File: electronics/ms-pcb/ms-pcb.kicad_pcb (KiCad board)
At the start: 2 copper layers, 110 x 110 mm, 25 parts, among them J1 Left motor, J2 Right motor, J3 XT60-M, U1 ESP32-S3-DEVKITC-1U-N8R2, U2 GY-521

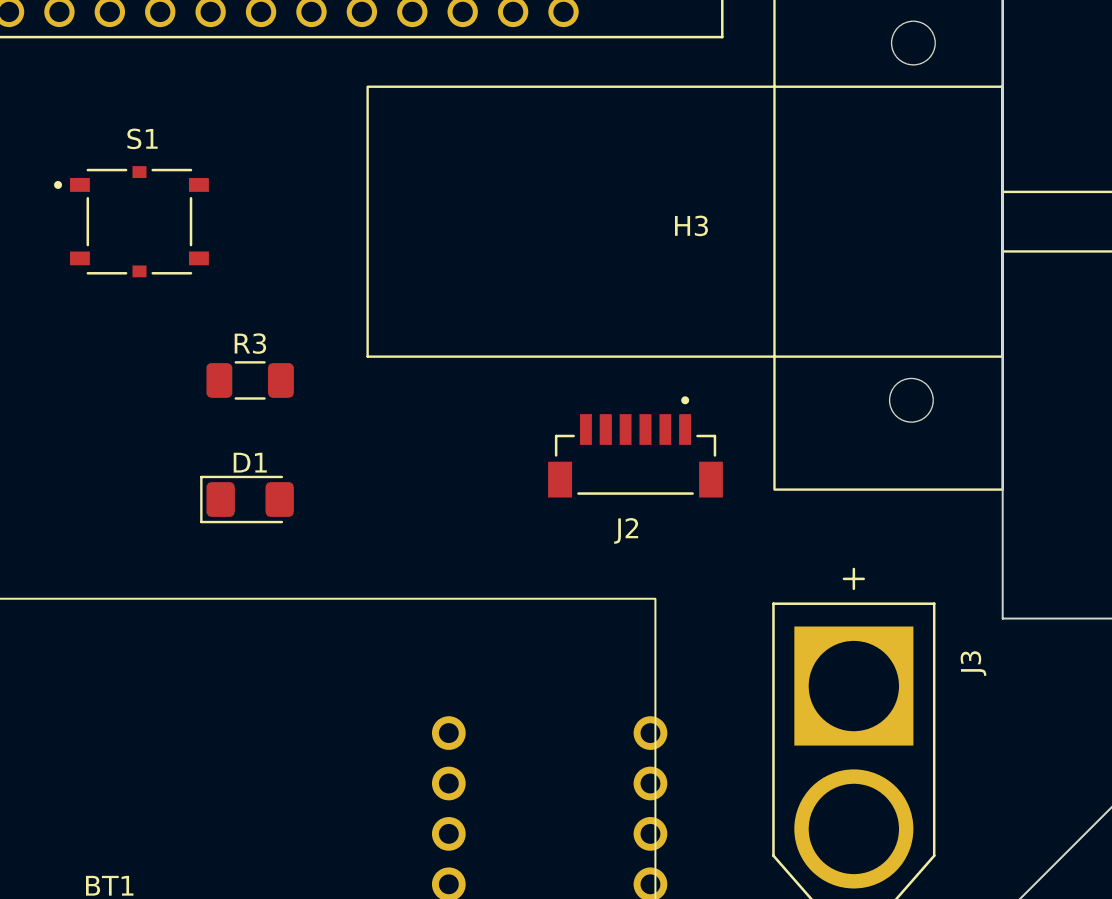
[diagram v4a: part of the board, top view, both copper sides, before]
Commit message: elec: enhance PCB v0.1 layout
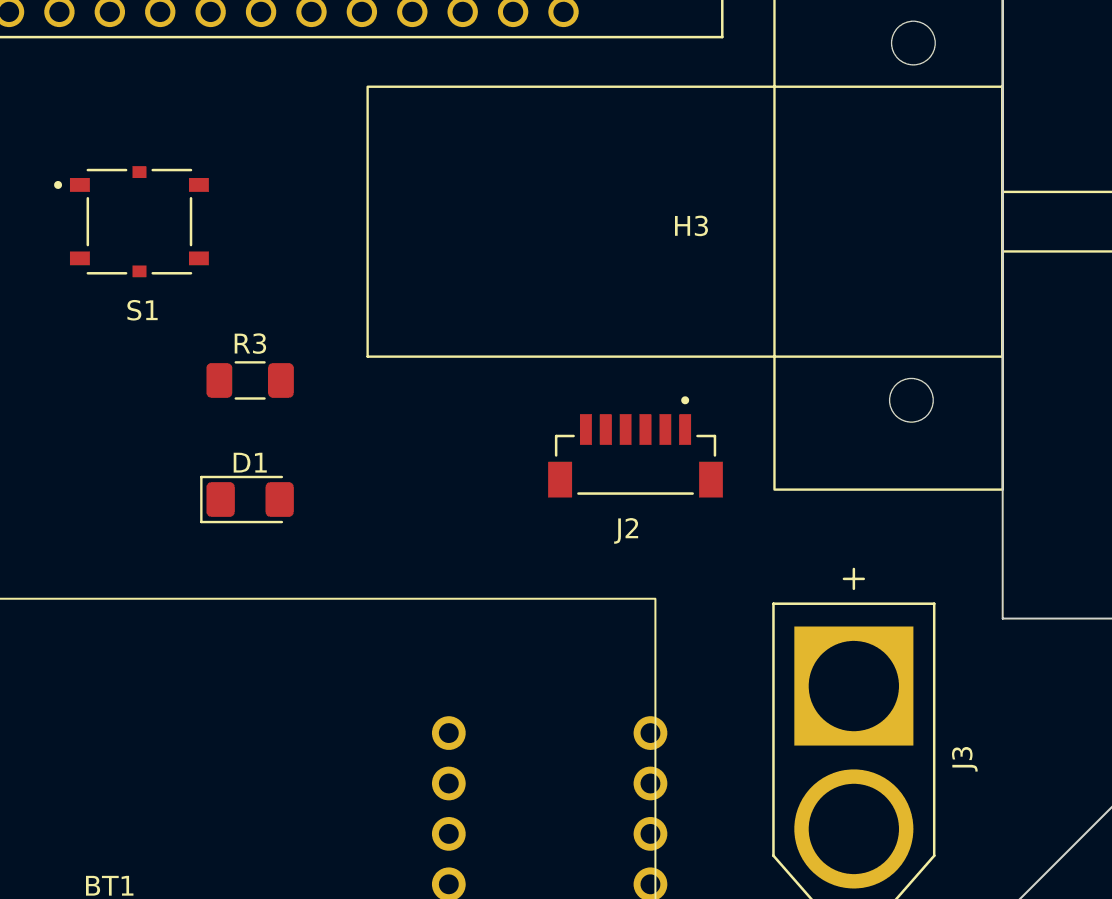
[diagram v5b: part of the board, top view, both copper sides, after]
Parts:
- H2, H4: footprint footprints:caster_wheel -> footprints:caster_wheel_custom
- renumbered DRV1 to DRV8833, LS1 to PKLCS1212E20A0-R1
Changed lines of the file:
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@@
 			)
 		)
-		(property "Description" ""
+		(property "Description" "\nConnector Header Surface Mount 6 position 0.039 (1.00mm)\n"
 			(at 98.500006 108.000013 0)
 			(layer "F.Fab")
@@
 			)
 		)
-		(property "Description" ""
+		(property "Description" "\nConnector Header Surface Mount 6 position 0.039 (1.00mm)\n"
 			(at 151.500002 108.000013 0)
 			(layer "F.Fab")
@@
 		(at 126.500001 94.999988)
 		(property "Reference" "S1"
-			(at 0.175 -4.135 0)
+			(at 0.175 4.500012 0)
 			(layer "F.SilkS")
 			(effects
@@
 		)
 		(property "Value" "PTS526_SMG15_SMTR2_LFS"
-			(at 12.875 4.135 0)
+			(at -0.000001 -4.499988 0)
 			(layer "F.Fab")
 			(effects
@@
 			)
 		)
-		(property "Description" ""
+		(property "Description" "\nTactile Switch SPST-NO Top Actuated Surface Mount\n"
 			(at 126.500001 94.999988 0)
 			(layer "F.Fab")
@@
 		(at 162.500005 122.00001 -90)
 		(property "Reference" "J3"
-			(at -4.825 -5.935 90)
+			(at -0.00001 -5.499995 90)
 			(layer "F.SilkS")
 			(effects
@@
 			)
 		)
-		(property "Description" ""
+		(property "Description" "\nPlug; DC supply; XT60; male; PIN: 2; for cable; soldered; 30A; 500V\n"
 			(at 162.500005 122.00001 0)
 			(layer "F.Fab")
@@
 			)
 		)
-		(property "Description" ""
+		(property "Description" "\nWiFi Development Tools - 802.11 ESP32-S3 Gen-Purpose Dev Bd, embeds ESP32-S3-WROOM-1U-N8R2, 8 MB Quad Flash, 2 MB Quad PSRAM, IPEX antenna connector, w/ Pin Header\n"
 			(at 124.500005 73.000006 0)
 			(layer "F.Fab")
@@
 		(at 97.5 122)
 		(property "Reference" "U2"
-			(at -2.885 9.445 0)
+			(at -3 12 0)
 			(layer "B.SilkS")
 			(effects
@@
 			)
 		)
-		(property "Description" ""
+		(property "Description" "\nTriple Axis Accelerometer Gyro Breakout\n"
 			(at 97.5 122 0)
 			(layer "F.Fab")
@@
 			(layer "B.SilkS")
 		)
-		(fp_text user "ITG/MPU"
-			(at -2.25 -11.51 0)
+		(fp_text user "MPU6080"
+			(at -3.5 -11.5 0)
 			(layer "B.SilkS")
 			(effects
@@
 		(tags "resistor handsolder")
 		(property "Reference" "R5"
-			(at 0 1.82 0)
+			(at 0 -2.5 0)
 			(layer "B.SilkS")
 			(effects
@@
 		)
 		(property "Value" "1k"
-			(at 0 -1.82 0)
+			(at 0 2.5 0)
 			(layer "B.Fab")
 			(effects
@@
 		)
 	)
-	(footprint "footprints:caster_wheel"
+	(footprint "footprints:caster_wheel_custom"
 		(locked yes)
 		(layer "B.Cu")
 		(at 124.5 51 180)
 		(property "Reference" "H2"
-			(at 0 1.4 -0)
+			(at 0.5 0 0)
 			(unlocked yes)
 			(layer "B.SilkS")
@@
 		)
 		(property "Value" "Caster_wheel_holes"
-			(at 0 0 0)
+			(at 0 -7 0)
 			(unlocked yes)
 			(layer "B.Fab")
@@
 			)
 		)
-		(property "Footprint" "footprints:caster_wheel"
+		(property "Footprint" "footprints:caster_wheel_custom"
 			(at 0 0 0)
 			(unlocked yes)
@@
 			)
 		)
+		(property ki_fp_filters "MountingHole*Pad*")
+		(sheetname "Root")
+		(sheetfile "ms-pcb.kicad_sch")
 		(attr through_hole)
 		(fp_circle
-			(center 8.000624 0)
-			(end 5.000624 0)
+			(center 8 0)
+			(end 10 0)
 			(stroke
-				(width 0.12)
-				(type solid)
+				(width 0.1)
+				(type default)
 			)
 			(fill none)
@@
 		(fp_circle
 			(center 0 0)
-			(end -8 -0.1)
+			(end 6 0)
 			(stroke
-				(width 0.12)
-				(type solid)
+				(width 0.1)
+				(type default)
 			)
 			(fill none)
@@
 		)
 		(fp_circle
-			(center -8 0.001666)
-			(end -11 0.001666)
+			(center -8 0)
+			(end -6 0)
 			(stroke
-				(width 0.12)
-				(type solid)
+				(width 0.1)
+				(type default)
 			)
 			(fill none)
@@
 		)
 		(fp_text user "${REFERENCE}"
-			(at 0 -1.6 0)
+			(at 0 -8.6 0)
 			(unlocked yes)
 			(layer "B.Fab")
@@
 			)
 		)
-		(dimension
-			(type aligned)
-			(layer "Cmts.User")
-			(pts
-				(xy 132.45 51) (xy 116.45 51)
-			)
-			(height 11)
-			(gr_text "16.0000 mm"
-				(at 124.45 38.9 0)
-				(layer "Cmts.User")
-				(effects
-					(font
-						(size 1 1)
-						(thickness 0.1)
-					)
-				)
-			)
-			(format
-				(prefix "")
-				(suffix "")
-				(units 3)
-				(units_format 1)
-				(precision 4)
-			)
-			(style
-				(thickness 0.1)
-				(arrow_length 1.27)
-				(text_position_mode 0)
-				(extension_height 0.58642)
-				(extension_offset 0.5) keep_text_aligned)
-		)
 		(pad "" np_thru_hole circle
 			(at -7.95 0 180)
@@
 		)
 		(group ""
-			(members "893cd183-fb31-4624-bc99-e0190041e662" "d2ef70d8-e3e8-4ba7-b9f9-4c512ddbdae9"
-				"db8d73bb-c116-4ba6-a0ca-7239095e6ff5"
+			(members "1334dab3-1a59-4aa6-96f0-a56ff0c46b70" "14df942f-8b17-49d6-8af2-d315b7768a5c"
+				"64fc95bb-4b9b-4163-b631-993261532cc8"
 			)
 		)
 		(group ""
-			(members "0ba887b9-25be-48d5-8c08-bb787daaddd3" "a9afcd08-4600-473d-b7d8-37a8b6542202"
-				"f1394a61-58e5-4641-94eb-1675498ff4fd"
+			(members "79962c2a-9342-4669-909b-a5eea195d1a0" "e2b0e38f-6582-4649-96f2-3fa585450b63"
+				"ef9e4861-e4fa-4bee-a0bc-1922cc89708f"
 			)
 		)
-		(model "${KIPRJMOD}/3dModels/caster-wheel-spacer.STEP"
+		(model "${KIPRJMOD}/3dModels/caster-wheel-custom.STEP"
 			(offset
 				(xyz 0 0 0)
@@
 			)
 		)
-		(model "${KIPRJMOD}/3dModels/caster ball wheel.STEP"
-			(offset
-				(xyz 0 0 1)
-			)
-			(scale
-				(xyz 1 1 1)
-			)
-			(rotate
-				(xyz 0 0 0)
-			)
-		)
 	)
-	(footprint "footprints:caster_wheel"
+	(footprint "footprints:caster_wheel_custom"
 		(locked yes)
 		(layer "B.Cu")
 		(at 124.5 139 180)
 		(property "Reference" "H4"
-			(at 0 1.4 -0)
+			(at 0.5 0 0)
 			(unlocked yes)
 			(layer "B.SilkS")
@@
 		)
 		(property "Value" "Caster_wheel_holes"
-			(at 0 0 0)
+			(at 0 -7 0)
 			(unlocked yes)
 			(layer "B.Fab")
@@
 			)
 		)
-		(property "Footprint" "footprints:caster_wheel"
+		(property "Footprint" "footprints:caster_wheel_custom"
 			(at 0 0 0)
 			(unlocked yes)
@@
 			)
 		)
+		(property ki_fp_filters "MountingHole*Pad*")
+		(sheetname "Root")
+		(sheetfile "ms-pcb.kicad_sch")
 		(attr through_hole)
 		(fp_circle
-			(center 8.000624 0)
-			(end 5.000624 0)
+			(center 8 0)
+			(end 10 0)
 			(stroke
-				(width 0.12)
-				(type solid)
+				(width 0.1)
+				(type default)
 			)
 			(fill none)
@@
 		(fp_circle
 			(center 0 0)
-			(end -8 -0.1)
+			(end 6 0)
 			(stroke
-				(width 0.12)
-				(type solid)
+				(width 0.1)
+				(type default)
 			)
 			(fill none)
@@
 		)
 		(fp_circle
-			(center -8 0.001666)
-			(end -11 0.001666)
+			(center -8 0)
+			(end -6 0)
 			(stroke
-				(width 0.12)
-				(type solid)
+				(width 0.1)
+				(type default)
 			)
 			(fill none)
@@
 		)
 		(fp_text user "${REFERENCE}"
-			(at 0 -1.6 0)
+			(at 0 -8.6 0)
 			(unlocked yes)
 			(layer "B.Fab")
@@
 			)
 		)
-		(dimension
-			(type aligned)
-			(layer "Cmts.User")
-			(pts
-				(xy 132.45 139) (xy 116.45 139)
-			)
-			(height 11)
-			(gr_text "16.0000 mm"
-				(at 124.45 126.9 0)
-				(layer "Cmts.User")
-				(effects
-					(font
-						(size 1 1)
-						(thickness 0.1)
-					)
-				)
-			)
-			(format
-				(prefix "")
-				(suffix "")
-				(units 3)
-				(units_format 1)
-				(precision 4)
-			)
-			(style
-				(thickness 0.1)
-				(arrow_length 1.27)
-				(text_position_mode 0)
-				(extension_height 0.58642)
-				(extension_offset 0.5) keep_text_aligned)
-		)
 		(pad "" np_thru_hole circle
 			(at -7.95 0 180)
@@
 		)
 		(group ""
-			(members "3bba315f-e47a-4b85-92a0-443aec8474a0" "65c76813-461f-47cb-a724-77987fa025ba"
-				"82b0ded0-ec8b-4c65-af79-4cf09b032e63"
+			(members "3c1a325d-10ab-48cb-b2ef-8c90b5043f20" "5959c696-1f39-4ba6-8ee1-5e14e6330a1a"
+				"a54a2343-533f-426b-b476-865ce082d00d"
 			)
 		)
 		(group ""
-			(members "0e00254e-8f56-40e0-b552-75ba5def1eec" "4ca7ede2-0112-470d-9f5e-42d19761b722"
-				"bf1098cd-715e-4d4d-89fd-1395c4704a90"
+			(members "1cab1e0d-8853-4d24-932c-8d59ed0eb0c4" "864c66a1-d970-4cbb-94a9-cce935dd0bd3"
+				"e3db144d-5aae-4f1d-a68b-2a67ec9323f6"
 			)
 		)
-		(model "${KIPRJMOD}/3dModels/caster-wheel-spacer.STEP"
+		(model "${KIPRJMOD}/3dModels/caster-wheel-custom.STEP"
 			(offset
 				(xyz 0 0 0)
@@
 			)
 		)
-		(model "${KIPRJMOD}/3dModels/caster ball wheel.STEP"
-			(offset
-				(xyz 0 0 1)
-			)
-			(scale
-				(xyz 1 1 1)
-			)
-			(rotate
-				(xyz 0 0 0)
-			)
-		)
 	)
 	(footprint "footprints:SPKR_PKLCS1212E20A0-R1"
 		(layer "B.Cu")
 		(at 110.49 72.39 180)
-		(property "Reference" "LS1"
-			(at -3.325 7.135 0)
+		(property "Reference" "PKLCS1212E20A0-R1"
+			(at -0.01 7.135 0)
 			(layer "B.SilkS")
 			(effects
@@
 			)
 		)
-		(property "Description" ""
+		(property "Description" "\nBuzzers Transducer, Externally Driven Piezo 1.5 V - 2kHz 70dB @ 1.5V, 10cm Surface Mount Solder Pads\n"
 			(at 110.49 72.39 0)
 			(layer "F.Fab")
@@
 		(tags "resistor handsolder")
 		(property "Reference" "R2"
-			(at 0 1.82 0)
+			(at 0 2.5 0)
 			(layer "B.SilkS")
 			(effects
@@
 		(layer "B.Cu")
 		(at 147.32 129.54)
-		(property "Reference" "DRV1"
+		(property "Reference" "DRV8833"
 			(at 0 11.684 180)
 			(unlocked yes)
@@
 		)
 	)
+	(gr_circle
+		(center 93 50.5)
+		(end 95 50.5)
+		(locked yes)
+		(stroke
+			(width 0.1)
+			(type default)
+		)
+		(fill none)
+		(layer "Dwgs.User")
+	)
+	(gr_circle
+		(center 73.5 70)
+		(end 75.5 70)
+		(locked yes)
+		(stroke
+			(width 0.1)
+			(type default)
+		)
+		(fill none)
+		(layer "Dwgs.User")
+	)
 	(gr_rect
 		(start 97.500008 114.000001)
@@
 		)
 		(fill none)
+		(layer "Dwgs.User")
+	)
+	(gr_circle
+		(center 112 43)
+		(end 114 43)
+		(locked yes)
+		(stroke
+			(width 0.1)
+			(type default)
+		)
+		(fill none)

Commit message: elec: PCB layout wiring
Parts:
- added H5: Bumper_front, footprints:Micromouse_bumper, F.Cu at (125.0, 40.0)
- added H6: Bumper_back, footprints:Micromouse_bumper, F.Cu at (125.0, 150.0)
- moved DRV1 26.1 mm to (125.0, 116.0), turned to -90 degrees
- moved LS1 22.9 mm to (103.0, 94.0)
- moved R2 21.5 mm to (153.7, 89.5), turned to 90 degrees
- moved R5 19.6 mm to (158.8, 89.5), turned to -90 degrees
- moved D1 5.24 mm to (130.5, 104.0)
- moved D2 5.02 mm to (117.5, 104.0), turned to 180 degrees
- moved R1 4.45 mm to (117.0, 91.5), turned to 90 degrees
- moved R3 4.32 mm to (130.4, 99.0)
- moved R4 4.02 mm to (117.5, 99.0), turned to 180 degrees
- moved S1 3.35 mm to (125.0, 92.0)
- moved U1 2.83 mm to (126.5, 71.0), turned to -90 degrees
- moved H2 0.50 mm to (125.0, 51.0)
- moved H4 0.50 mm to (125.0, 139.0)
- renumbered DRV8833 to DRV1, PKLCS1212E20A0-R1 to LS1
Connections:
- U1 pad J1_10: DRV_R1 -> unconnected-(U1-GPIO17-PadJ1_10)
- U1 pad J1_11: DRV_R2 -> unconnected-(U1-GPIO18-PadJ1_11)
- U1 pad J1_13: buzzer -> unconnected-(U1-GPIO3-PadJ1_13)
- U1 pad J1_16: button -> XSHUT_FR
- U1 pad J1_17: unconnected-(U1-GPIO11-PadJ1_17) -> XSHUT_R
- U1 pad J1_18: unconnected-(U1-GPIO12-PadJ1_18) -> XSHUT_F
- U1 pad J1_19: unconnected-(U1-GPIO13-PadJ1_19) -> XSHUT_L
- U1 pad J1_20: unconnected-(U1-GPIO14-PadJ1_20) -> XSHUT_FL
- U1 pad J1_4: ENC_L1 -> SDA
- U1 pad J1_5: ENC_L2 -> SCL
- U1 pad J1_6: ENC_R1 -> unconnected-(U1-GPIO6-PadJ1_6)
- U1 pad J1_7: ENC_R2 -> unconnected-(U1-GPIO7-PadJ1_7)
- U1 pad J1_8: DRV_L1 -> unconnected-(U1-GPIO15-PadJ1_8)
- U1 pad J1_9: DRV_L2 -> unconnected-(U1-GPIO16-PadJ1_9)
- U1 pad J3_10: XSHUT_R -> DRV_R1
- U1 pad J3_11: unconnected-(U1-GPIO37-PadJ3_11) -> DRV_R2
- U1 pad J3_12: unconnected-(U1-GPIO36-PadJ3_12) -> DRV_L2
- U1 pad J3_13: unconnected-(U1-GPIO35-PadJ3_13) -> DRV_L1
- U1 pad J3_16: unconnected-(U1-GPIO48-PadJ3_16) -> buzzer
- U1 pad J3_17: unconnected-(U1-GPIO47-PadJ3_17) -> button
- U1 pad J3_18: unconnected-(U1-GPIO21-PadJ3_18) -> ENC_L2
- U1 pad J3_19: unconnected-(U1-USB_D+/GPIO20-PadJ3_19) -> Vmes
- U1 pad J3_20: unconnected-(U1-USB_D-/GPIO19-PadJ3_20) -> ENC_L1
- U1 pad J3_4: SDA -> unconnected-(U1-GPIO1-PadJ3_4)
- U1 pad J3_5: SCL -> unconnected-(U1-GPIO2-PadJ3_5)
- U1 pad J3_6: XSHUT_L -> ENC_R2
- U1 pad J3_7: XSHUT_FL -> ENC_R1
- U1 pad J3_8: XSHUT_F -> unconnected-(U1-MTDO/GPIO40-PadJ3_8)
- U1 pad J3_9: XSHUT_FR -> unconnected-(U1-MTCK/GPIO39-PadJ3_9)
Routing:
- net +BATT: track 0.00 -> 193.4 mm, vias 0 -> 1
- net SCL: track 0.00 -> 185.9 mm, vias 0 -> 1
- net SDA: track 0.00 -> 175.3 mm, vias 0 -> 1
- net Vmes: track 0.00 -> 59.5 mm, vias 0 -> 1
- net XSHUT_R: track 0.00 -> 44.0 mm, vias 0 -> 2
- net XSHUT_FR: track 0.00 -> 43.6 mm, vias 0 -> 2
- net MOT_R2: track 0.00 -> 40.2 mm
- net MOT_R1: track 0.00 -> 35.9 mm
- net MOT_L2: track 0.00 -> 34.3 mm
- net XSHUT_FL: track 0.00 -> 34.1 mm
- net MOT_L1: track 0.00 -> 33.3 mm
- net DRV_R2: track 0.00 -> 30.3 mm
- net DRV_L1: track 0.00 -> 30.3 mm
- net DRV_R1: track 0.00 -> 30.3 mm
- net DRV_L2: track 0.00 -> 30.1 mm
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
